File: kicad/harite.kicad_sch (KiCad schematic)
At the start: 78 parts, among them J1 503480-0500, J2 Wired Joystick, J4 5034801200, J5 5034801200, U1 RP2040_Zero, U2 RP2040_Zero

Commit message: add joycon
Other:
- moved on the sheet: H5
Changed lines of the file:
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@@
 	(symbol
 		(lib_id "ScottoKeebs:Placeholder_Mounting_Hole")
-		(at 113.03 127 0)
+		(at 111.76 128.27 0)
 		(unit 1)
 		(exclude_from_sim no)
@@
 		(fields_autoplaced yes)
 		(property "Reference" "H5"
-			(at 115.57 125.7299 0)
+			(at 114.3 126.9999 0)
 			(effects
 				(font
@@
 		)
 		(property "Value" "Mounting_Hole"
-			(at 115.57 128.2699 0)
+			(at 114.3 129.5399 0)
 			(effects
 				(font
@@
 		)
 		(property "Footprint" "MountingHole:MountingHole_2.2mm_M2_Pad_Via"
-			(at 113.03 127 0)
+			(at 111.76 128.27 0)
 			(effects
 				(font
@@
 		)
 		(property "Datasheet" "~"
-			(at 113.03 127 0)
+			(at 111.76 128.27 0)
 			(effects
 				(font
@@
 		)
 		(property "Description" "Mounting Hole without connection"
-			(at 113.03 127 0)
+			(at 111.76 128.27 0)
 			(effects
 				(font
@@
 	)
 	(symbol
-		(lib_id "ScottoKeebs:Placeholder_Mounting_Hole")
-		(at 120.65 243.84 0)
-		(unit 1)
-		(exclude_from_sim no)
-		(in_bom yes)
-		(on_board yes)
-		(dnp no)
-		(fields_autoplaced yes)
-		(property "Reference" "H9"
-			(at 123.19 242.5699 0)
-			(effects
-				(font
-					(size 1.27 1.27)
-				)
-				(justify left)
-			)
-		)
-		(property "Value" "Mounting_Hole"
-			(at 123.19 245.1099 0)
-			(effects
-				(font
-					(size 1.27 1.27)
-				)
-				(justify left)
-			)
-		)
-		(property "Footprint" "MountingHole:MountingHole_2.2mm_M2_Pad_Via"
-			(at 120.65 243.84 0)
-			(effects
-				(font
-					(size 1.27 1.27)
-				)
-				(hide yes)
-			)
-		)
-		(property "Datasheet" "~"
-			(at 120.65 243.84 0)
-			(effects
-				(font
-					(size 1.27 1.27)
-				)
-				(hide yes)
-			)
-		)
-		(property "Description" "Mounting Hole without connection"
-			(at 120.65 243.84 0)
-			(effects
-				(font
-					(size 1.27 1.27)
-				)
-				(hide yes)
-			)
-		)
-		(instances
-			(project "harite"
-				(path "/feb70c3f-3e34-4f8f-9694-07d231f2d237"
-					(reference "H9")
-					(unit 1)
-				)
-			)
-		)
-	)
-	(symbol
 		(lib_id "Device:D")
 		(at 163.83 60.96 0)
@@
 	)
 	(symbol
-		(lib_id "ScottoKeebs:Placeholder_Mounting_Hole")
-		(at 120.65 248.92 0)
-		(unit 1)
-		(exclude_from_sim no)
-		(in_bom yes)
-		(on_board yes)
-		(dnp no)
-		(fields_autoplaced yes)
-		(property "Reference" "H10"
-			(at 123.19 247.6499 0)
-			(effects
-				(font
-					(size 1.27 1.27)
-				)
-				(justify left)
-			)
-		)
-		(property "Value" "Mounting_Hole"
-			(at 123.19 250.1899 0)
-			(effects
-				(font
-					(size 1.27 1.27)
-				)
-				(justify left)
-			)
-		)
-		(property "Footprint" "MountingHole:MountingHole_2.2mm_M2_Pad_Via"
-			(at 120.65 248.92 0)
-			(effects
-				(font
-					(size 1.27 1.27)
-				)
-				(hide yes)
-			)
-		)
-		(property "Datasheet" "~"
-			(at 120.65 248.92 0)
-			(effects
-				(font
-					(size 1.27 1.27)
-				)
-				(hide yes)
-			)
-		)
-		(property "Description" "Mounting Hole without connection"
-			(at 120.65 248.92 0)
-			(effects
-				(font
-					(size 1.27 1.27)
-				)
-				(hide yes)
-			)
-		)
-		(instances
-			(project "harite"
-				(path "/feb70c3f-3e34-4f8f-9694-07d231f2d237"
-					(reference "H10")
-					(unit 1)
-				)
-			)
-		)
-	)
-	(symbol
 		(lib_id "Device:D")
 		(at 276.86 60.96 180)
@@
 	)
 	(symbol
+		(lib_id "ScottoKeebs:Placeholder_Mounting_Hole")
+		(at 120.65 243.84 0)
+		(unit 1)
+		(exclude_from_sim no)
+		(in_bom yes)
+		(on_board yes)
+		(dnp no)
+		(fields_autoplaced yes)
+		(property "Reference" "H9"
+			(at 123.19 242.5699 0)
+			(effects
+				(font
+					(size 1.27 1.27)
+				)
+				(justify left)
+			)
+		)
+		(property "Value" "Mounting_Hole"
+			(at 123.19 245.1099 0)
+			(effects
+				(font
+					(size 1.27 1.27)
+				)
+				(justify left)
+			)
+		)
+		(property "Footprint" "MountingHole:MountingHole_2.2mm_M2_Pad_Via"
+			(at 120.65 243.84 0)
+			(effects
+				(font
+					(size 1.27 1.27)
+				)
+				(hide yes)
+			)
+		)
+		(property "Datasheet" "~"
+			(at 120.65 243.84 0)
+			(effects
+				(font
+					(size 1.27 1.27)
+				)
+				(hide yes)
+			)
+		)
+		(property "Description" "Mounting Hole without connection"
+			(at 120.65 243.84 0)
+			(effects
+				(font
+					(size 1.27 1.27)
+				)
+				(hide yes)
+			)
+		)
+		(instances
+			(project "harite"
+				(path "/feb70c3f-3e34-4f8f-9694-07d231f2d237"
+					(reference "H9")
+					(unit 1)
+				)
+			)
+		)
+	)
+	(symbol
 		(lib_id "SKRHADE010:SKRHADE010")
 		(at 243.84 241.3 0)
@@
 					(unit 1)
 				)
+			)
+		)
+	)
+	(symbol
+		(lib_id "ScottoKeebs:Placeholder_Mounting_Hole")
+		(at 120.65 248.92 0)
+		(unit 1)
+		(exclude_from_sim no)
+		(in_bom yes)
+		(on_board yes)
+		(dnp no)
+		(fields_autoplaced yes)
+		(property "Reference" "H10"
+			(at 123.19 247.6499 0)
+			(effects
+				(font
+					(size 1.27 1.27)
+				)
+				(justify left)
+			)
+		)
+		(property "Value" "Mounting_Hole"
+			(at 123.19 250.1899 0)
+			(effects
+				(font
+					(size 1.27 1.27)
+				)
+				(justify left)
+			)
+		)
+		(property "Footprint" "MountingHole:MountingHole_2.2mm_M2_Pad_Via"
+			(at 120.65 248.92 0)
+			(effects
+				(font
+					(size 1.27 1.27)
+				)
+				(hide yes)
+			)
+		)
+		(property "Datasheet" "~"
+			(at 120.65 248.92 0)
+			(effects
+				(font
+					(size 1.27 1.27)
+				)
+				(hide yes)
+			)
+		)
+		(property "Description" "Mounting Hole without connection"
+			(at 120.65 248.92 0)
+			(effects
+				(font
+					(size 1.27 1.27)
+				)
+				(hide yes)
+			)
+		)
+		(instances
+			(project "harite"
+				(path "/feb70c3f-3e34-4f8f-9694-07d231f2d237"
+					(reference "H10")
+					(unit 1)
+				)

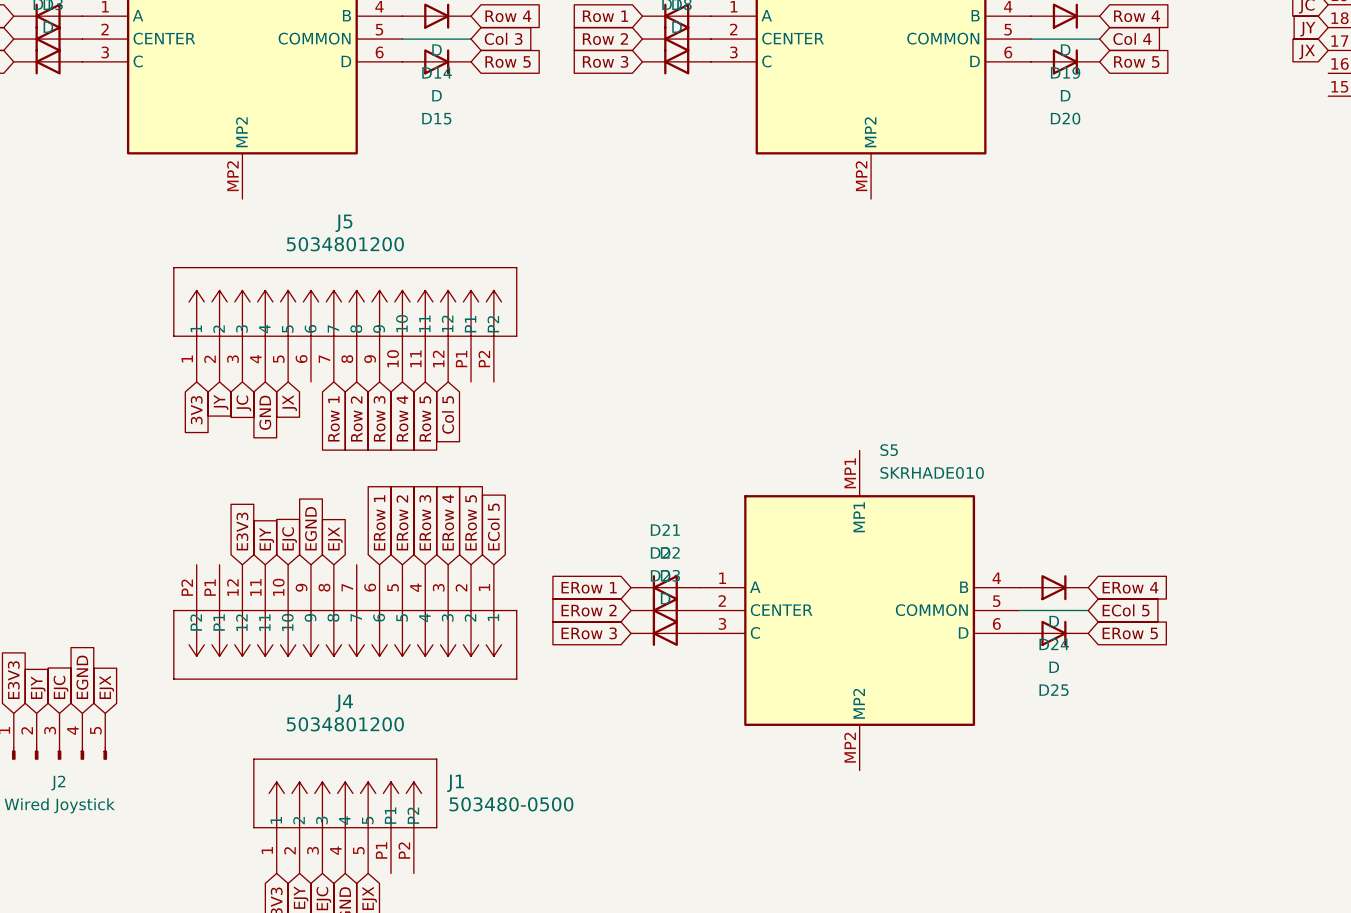
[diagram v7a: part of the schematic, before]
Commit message: move diodes
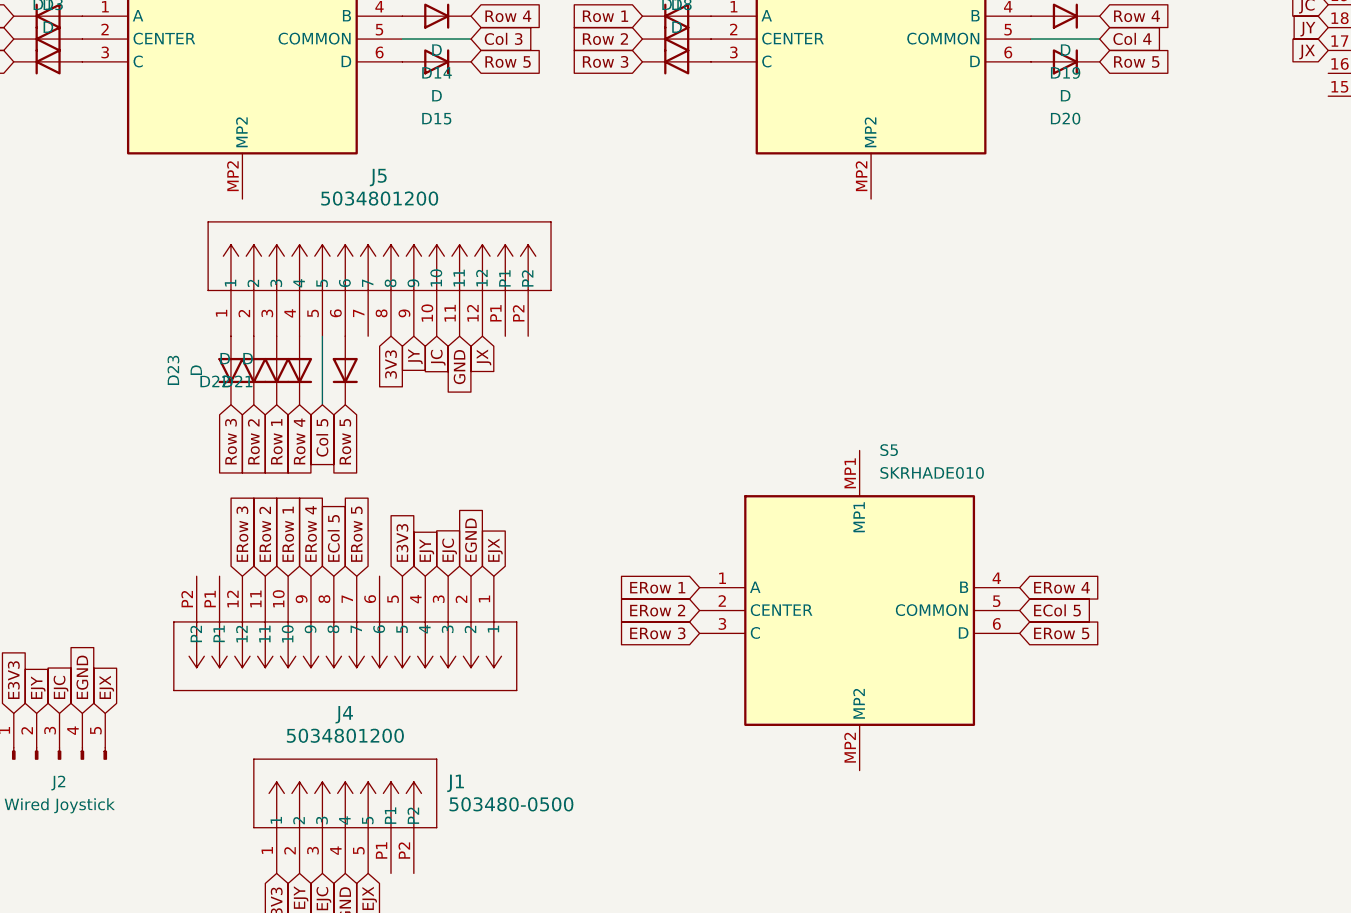
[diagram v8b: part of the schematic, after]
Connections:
- net 3V3: now also J5.8; no longer J5.1
- net Col 5: now also J5.5; no longer J5.12
- net E3V3: now also J4.5; no longer J4.12
- net ECol 5: now also J4.8; no longer J4.1
- net EGND: now also J4.2; no longer J4.9
- net EJC: now also J4.3; no longer J4.10
- net EJX: now also J4.1; no longer J4.8
- net EJY: now also J4.4; no longer J4.11
- net ERow 1: now also J4.10, S5.1 (A); no longer D21.1 (K), J4.6
- net ERow 2: now also J4.11, S5.2 (CENTER); no longer D22.1 (K), J4.5
- net ERow 3: now also J4.12, S5.3 (C); no longer D23.1 (K), J4.4
- net ERow 4: now also J4.9, S5.4 (B); no longer D24.1 (K), J4.3
- net ERow 5: now also J4.7, S5.6 (D); no longer D25.1 (K), J4.2
- net GND: now also J5.11; no longer J5.4
- net JC: now also J5.10; no longer J5.3
- net JX: now also J5.12; no longer J5.5
- net JY: now also J5.9; no longer J5.2
- net Row 1: now also D21.1 (K); no longer J5.7
- net Row 2: now also D22.1 (K); no longer J5.8
- net Row 3: now also D23.1 (K); no longer J5.9
- net Row 4: now also D24.1 (K); no longer J5.10
- net Row 5: now also D25.1 (K); no longer J5.11
- net at D23.2 (A): now also J5.1; no longer S5.3 (C)
- net at D22.2 (A): now also J5.2; no longer S5.2 (CENTER)
- net at D21.2 (A): now also J5.3; no longer S5.1 (A)
- net at D24.2 (A): now also J5.4; no longer S5.4 (B)
- net at D25.2 (A): now also J5.6; no longer S5.6 (D)
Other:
- moved on the sheet: J4, J5
